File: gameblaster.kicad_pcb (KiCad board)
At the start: 2 copper layers, 136.7 x 109.8 mm, 74 parts, among them IC1 TEA2025, IC10 74LS125, IC12 74LS74, IC2 SAA1099, IC3 SAA1099, IC4 74LS245, IC5 74LS374, IC6 74LS138, IC7 74LS138, IC8 74LS32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

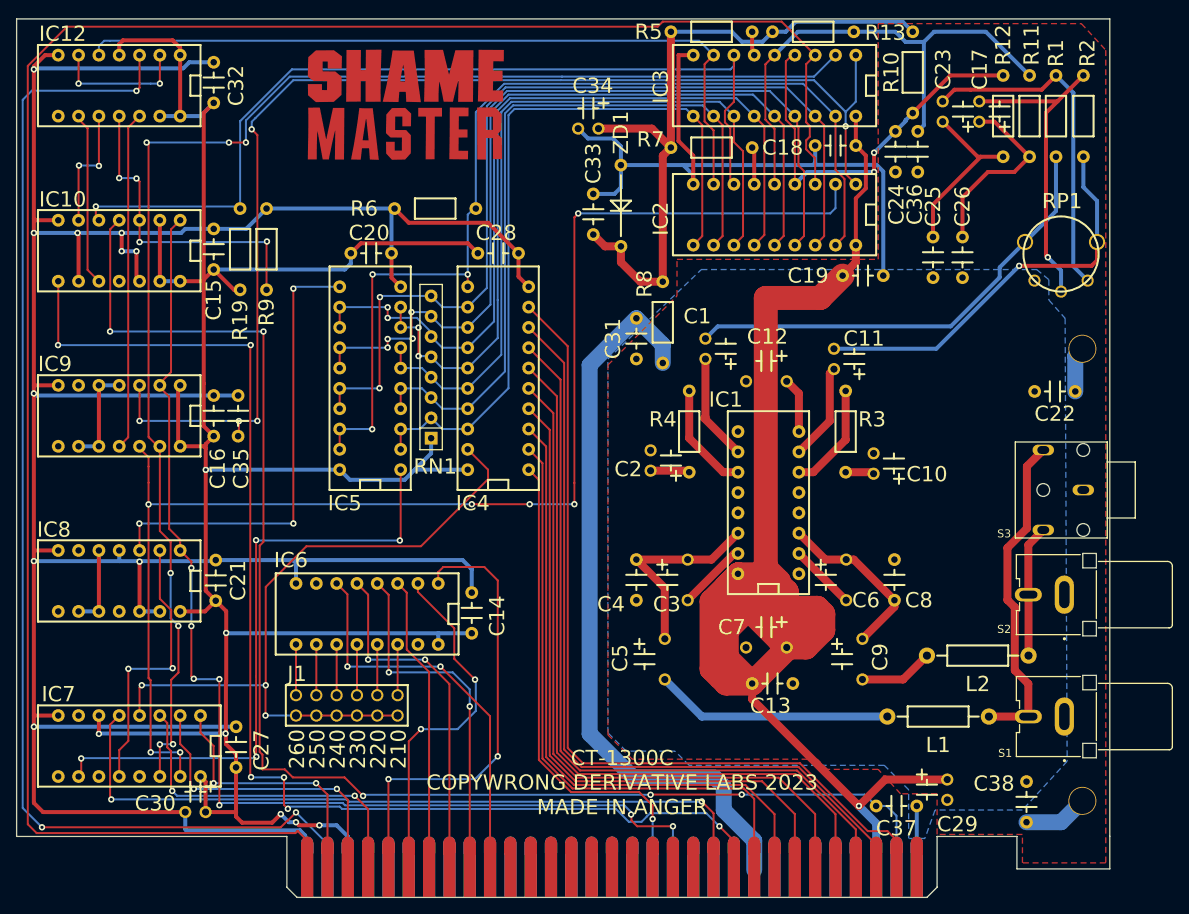
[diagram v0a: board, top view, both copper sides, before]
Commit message: fuck it let's add a big old digital ground plane
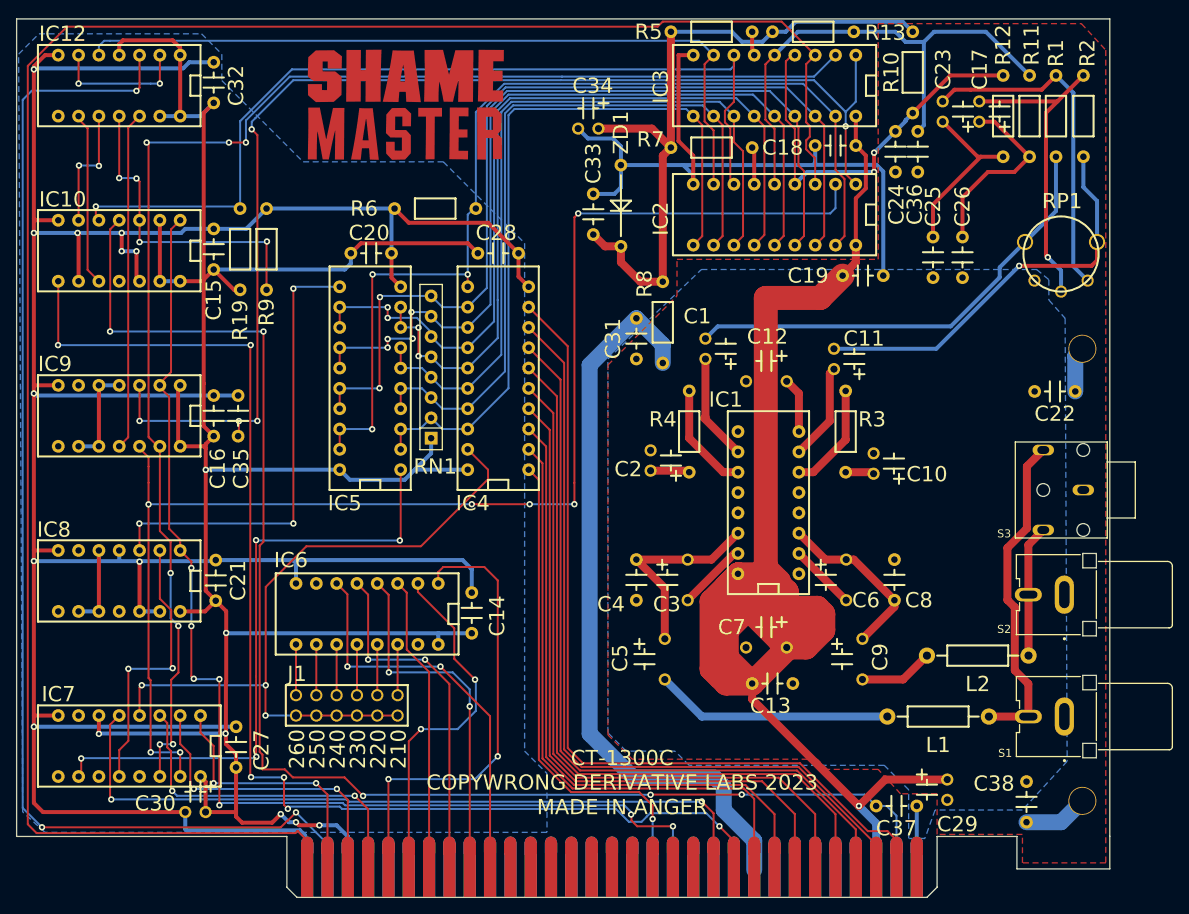
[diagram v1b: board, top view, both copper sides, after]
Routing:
- added copper zone on B.Cu, net GND
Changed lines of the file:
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@@
+    )
+  )
+  (zone (net 108) (net_name "GND") (layer "B.Cu") (hatch edge 0.508)
+    (connect_pads (clearance 0.508))
+    (min_thickness 0.254) (filled_areas_thickness no)
+    (fill yes (thermal_gap 0.508) (thermal_bridge_width 0.508))
+    (polygon
+      (pts
+        (xy 86.36 33.02)
+        (xy 86.36 36.322)
+        (xy 96.52 46.482)
+        (xy 114.046 46.482)
+        (xy 124.206 56.642)
+        (xy 124.206 120.142)
+        (xy 127 122.936)
+        (xy 127 130.302)
+        (xy 64.262 130.302)
+        (xy 61.468 127.762)
+        (xy 60.96 33.02)
+        (xy 63.5 30.48)
+        (xy 83.82 30.48)
+      )
     )
   )

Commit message: update gerbil
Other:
- board text added: "Special Thanks: TubeTime - reverse engineering of the original Game Blaster PCB; many circuits borrowed; footprint library. Tronix - original transceiver/register logic for card detection Wings - analog section consultation leaded solder - generally being a shithead and encouraging my terrible ideas"
- board text removed: "Special Thanks: TubeTime - reverse engineering of the big stupid DIP-40; DTACK circuit and TEA2025B section from the Snark Barker; copious footprints and silkscreen Tronix - original transceiver/register logic for card detection leadedsolder - generally being a shithead and encouraging my terrible ideas"
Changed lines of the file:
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@@
     (effects (font (size 1 1) (thickness 0.2)) (justify mirror))
   )
-  (gr_text "Special Thanks:\nTubeTime - reverse engineering of the\n  big stupid DIP-40; DTACK circuit and\n  TEA2025B section from the Snark Barker;\n  copious footprints and silkscreen\nTronix - original transceiver/register\n  logic for card detection\nleadedsolder - generally being a \n  shithead and encouraging my terrible\n  ideas" (at 128.27 38.1) (layer "B.SilkS")
+  (gr_text "Special Thanks:\nTubeTime - reverse engineering of the\n  original Game Blaster PCB; many circuits\n  borrowed; footprint library.\nTronix - original transceiver/register\n  logic for card detection\nWings - analog section consultation\nleaded solder - generally being a \n  shithead and encouraging my terrible\n  ideas" (at 128.27 38.1) (layer "B.SilkS")
     (effects (font (size 0.9525 0.9525) (thickness 0.127)) (justify left mirror))
   )

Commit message: Fix some shit
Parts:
- added R14: 1K, gameblaster:RESA400, F.Cu at (88.6, 52.3)
- C1, C11: value 0.22uF 16V -> 10uF 16V
- C10, C2: value 22uF 16V -> 10uF 16V
- C17, C23: value 1uF tant -> 10uF tant
- C24, C36: value 680pF -> 1000pF
- C25, C26: value 680pF -> 2200pF
- moved R19 39.8 mm to (128.3, 58.9)
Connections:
- C4 pad 2: Net-(C3-Pad1) -> Net-(C3-Pad2)
- C5 pad 1: Net-(C3-Pad1) -> Net-(C3-Pad2)
- C6 pad 2: Net-(C6-Pad2) -> Net-(C8-Pad1)
- C8 pad 1: Net-(C6-Pad1) -> Net-(C8-Pad1)
- C9 pad 1: Net-(C6-Pad1) -> Net-(C8-Pad1)
- IC1 pad 2: Net-(C6-Pad2) -> Net-(C8-Pad1)
- R19 pad 1: VCC -> VDDA
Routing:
- net /~{DTACK}: track 113.8 -> 138.7 mm, vias 1 -> 3
- net Net-(IC10-Pad6): track 15.6 -> 38.6 mm, vias 2 -> 3
- net Net-(C8-Pad1): track 0.00 -> 20.1 mm
- net Net-(C3-Pad1): track 25.4 -> 7.65 mm
- net Net-(C6-Pad1): track 21.9 -> 7.27 mm
- net Net-(C3-Pad2): track 8.71 -> 23.2 mm
- net Net-(C6-Pad2): track 8.33 -> 0.00 mm
- net VDDA: track 86.3 -> 94.0 mm
- net VCC: track 307.1 -> 302.7 mm

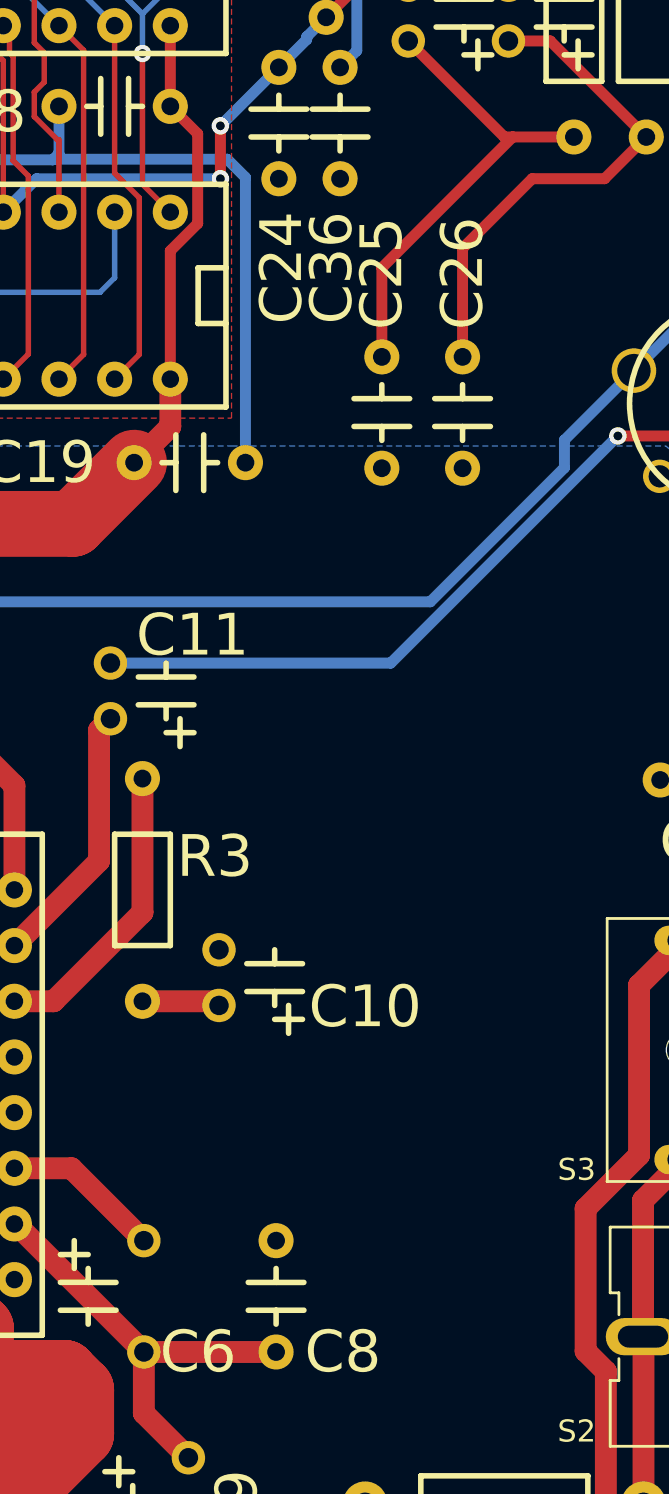
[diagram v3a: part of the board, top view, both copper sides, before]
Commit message: Add 3D models for Bracket and Volume pot/knob, update gerbers
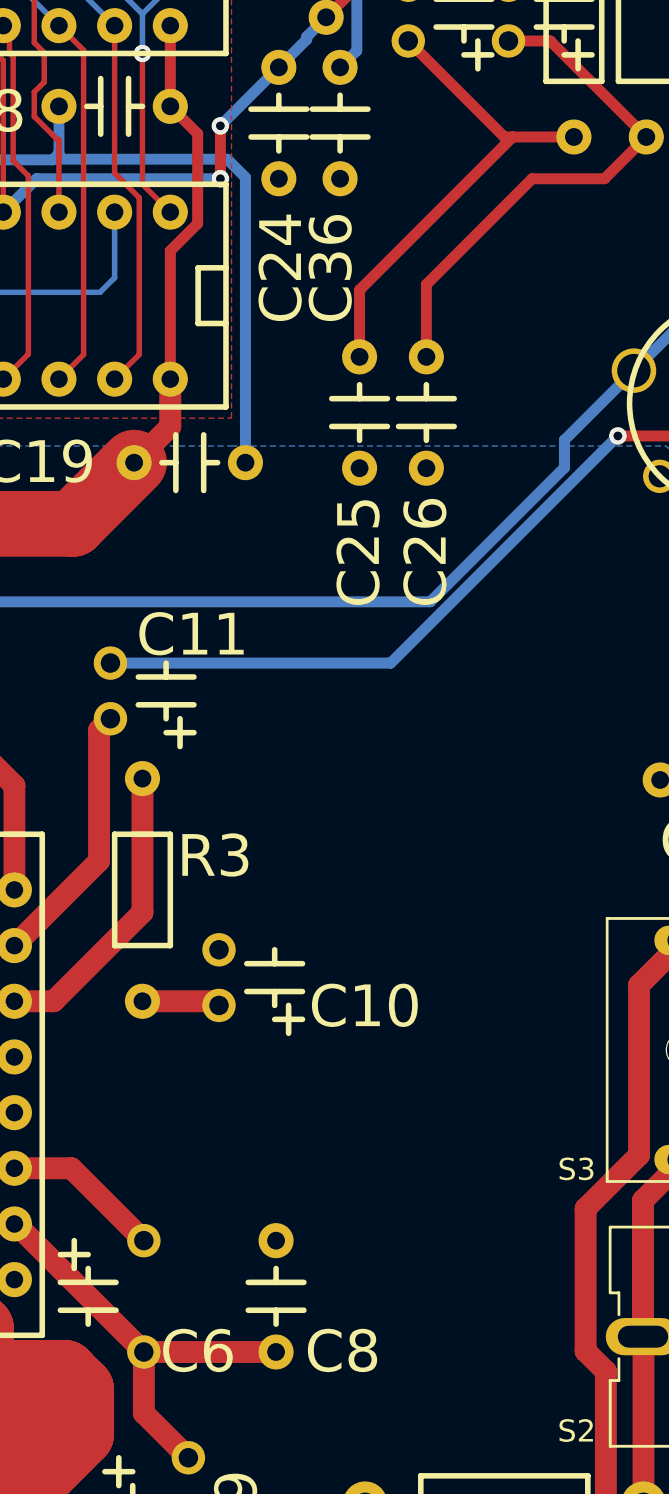
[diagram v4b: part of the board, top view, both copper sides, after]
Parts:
- C10, C2: value 10uF 16V -> 22uF 16V
- moved C26 1.65 mm to (177.3, 55.9)
- moved C25 1.02 mm to (174.2, 55.9)
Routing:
- net Net-(C17-Pad1): track 23.5 -> 24.2 mm
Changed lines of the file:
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@@
     (pad "1" thru_hole circle locked (at 0 56.515) (size 3.5 3.5) (drill 3.2766) (layers *.Cu *.Mask)
       (net 51 "/CHASSIS") (pinfunction "1") (pintype "input"))
-    (model "C:/Data/Projects/Adlib/mech/keystone 9202.wrl"
-      (offset (xyz 6.095999908 -88.26499867 6.476999903))
-      (scale (xyz 10 10 10))
-      (rotate (xyz 0 0 0))
+    (model "${KIPRJMOD}/packages3d/keystone-PN9202.STEP"
+      (offset (xyz 6.12 31.75 19.05))
+      (scale (xyz 1 1 1))
+      (rotate (xyz 0 180 90))
     )
   )
@@
     (pad "3B" thru_hole circle (at -3.323402 -3.323402 90) (size 1.524 1.524) (drill 1.016) (layers *.Cu *.Mask)
       (net 108 "Net-(C23-Pad2)") (pinfunction "3B") (pintype "passive"))
+    (model "${KIPRJMOD}/packages3d/RK08H12100F3.stp"
+      (offset (xyz 3.35 3.35 -0.125))
+      (scale (xyz 1 1 1))
+      (rotate (xyz 0 0 0))
+    )
+    (model "${KIPRJMOD}/packages3d/Volume-Knob-Recessed.step"
+      (offset (xyz 0 0 3.375))
+      (scale (xyz 1 1 1))
+      (rotate (xyz 0 0 0))
+    )
   )
   (footprint "gameblaster:RESA400" (layer "F.Cu")
@@
   )
   (footprint "gameblaster:CAPAC200" (layer "F.Cu")
-    (at 178.943 55.88 -90)
+    (at 177.292 55.88 -90)
     (property "Sheetfile" "gameblaster.kicad_sch")
     (property "Sheetname" "")
     (attr through_hole)
-    (fp_text reference "C26" (at -3.81 0 90) (layer "F.SilkS")
+    (fp_text reference "C26" (at 8.89 0 90) (layer "F.SilkS")
       (effects (font (size 1.905 1.905) (thickness 0.254)))
     )
@@
   )
   (footprint "gameblaster:CAPAC200" (layer "F.Cu")
-    (at 175.26 55.88 -90)
+    (at 174.244 55.88 -90)
     (property "Sheetfile" "gameblaster.kicad_sch")
     (property "Sheetname" "")
     (attr through_hole)
-    (fp_text reference "C25" (at -3.81 0 90) (layer "F.SilkS")
+    (fp_text reference "C25" (at 8.89 0 90) (layer "F.SilkS")
       (effects (font (size 1.905 1.905) (thickness 0.254)))
     )
@@
       (effects (font (size 1.905 1.905) (thickness 0.254)))
     )
-    (fp_text value "10uF 16V" (at 1.397 1.5875 90) (layer "F.Fab")
+    (fp_text value "22uF 16V" (at 1.397 1.5875 90) (layer "F.Fab")
       (effects (font (size 1 1) (thickness 0.15)))
     )
@@
       (effects (font (size 1.905 1.905) (thickness 0.254)))
     )
-    (fp_text value "10uF 16V" (at 1.27 -4.699 90) (layer "F.Fab")
+    (fp_text value "22uF 16V" (at 1.27 -4.699 90) (layer "F.Fab")
       (effects (font (size 1 1) (thickness 0.15)))
     )
@@
       (xy 113.880473 39.712815)
     ) (layer "F.Mask") (width 0) (fill solid))
-  (gr_circle (center 191.262 58.006) (end 201.512 58.006) (layer "Dwgs.User") (width 0.2) (fill none))
+  (gr_circle (center 191.262 58.006) (end 203.262 58.006) (layer "Dwgs.User") (width 0.2) (fill none))
   (gr_line (start 197.358 28.618) (end 60.706 28.618) (layer "Edge.Cuts") (width 0.15))
   (gr_line (start 175.768 137.16) (end 175.768 130.81) (layer "Edge.Cuts") (width 0.15))
@@
   (segment (start 158.496 80.2005) (end 158.496 75.438) (width 1) (layer "F.Cu") (net 49))
   (segment (start 158.496 75.438) (end 156.972 73.914) (width 1) (layer "F.Cu") (net 49))
-  (segment (start 182.118 47.752) (end 178.943 50.927) (width 0.5) (layer "F.Cu") (net 50))
-  (segment (start 178.943 50.927) (end 178.943 55.88) (width 0.5) (layer "F.Cu") (net 50))
-  (segment (start 181.0385 41.4655) (end 182.9435 41.4655) (width 0.5) (layer "F.Cu") (net 50))
-  (segment (start 182.9435 41.4655) (end 187.325 45.847) (width 0.5) (layer "F.Cu") (net 50))
   (segment (start 187.325 45.847) (end 185.42 47.752) (width 0.5) (layer "F.Cu") (net 50))
+  (segment (start 181.0385 41.4655) (end 182.9435 41.4655) (width 0.5) (layer "F.Cu") (net 50))
   (segment (start 185.42 47.752) (end 182.118 47.752) (width 0.5) (layer "F.Cu") (net 50))
+  (segment (start 182.9435 41.4655) (end 187.325 45.847) (width 0.5) (layer "F.Cu") (net 50))
+  (segment (start 177.292 52.578) (end 177.292 55.88) (width 0.5) (layer "F.Cu") (net 50))
+  (segment (start 182.118 47.752) (end 177.292 52.578) (width 0.5) (layer "F.Cu") (net 50))
   (segment (start 186.944 129.032) (end 191.262 129.032) (width 2) (layer "B.Cu") (net 51))
   (segment (start 193.04 70.739) (end 193.929 69.85) (width 2) (layer "B.Cu") (net 51))
@@
   (segment (start 181.229 45.847) (end 184.023 45.847) (width 0.5) (layer "F.Cu") (net 70))
   (segment (start 176.4665 41.4655) (end 180.848 45.847) (width 0.5) (layer "F.Cu") (net 70))
+  (segment (start 174.244 52.832) (end 174.244 55.88) (width 0.5) (layer "F.Cu") (net 70))
+  (segment (start 181.229 45.847) (end 174.244 52.832) (width 0.5) (layer "F.Cu") (net 70))
   (segment (start 180.848 45.847) (end 181.229 45.847) (width 0.5) (layer "F.Cu") (net 70))
-  (segment (start 175.26 55.88) (end 175.26 51.816) (width 0.5) (layer "F.Cu") (net 70))
-  (segment (start 175.26 51.816) (end 181.229 45.847) (width 0.5) (layer "F.Cu") (net 70))
   (segment (start 76.073 37.2364) (end 75.692 37.6174) (width 0.25) (layer "F.Cu") (net 71))
   (segment (start 76.073 33.147) (end 76.073 37.2364) (width 0.25) (layer "F.Cu") (net 71))
@@
   (segment (start 158.496 95.4405) (end 158.5595 95.4405) (width 1) (layer "F.Cu") (net 131))
   (segment (start 164.4015 101.2825) (end 170.434 101.2825) (width 1) (layer "F.Cu") (net 131))
-  (segment (start 164.4015 101.2825) (end 164.338 101.2825) (width 1) (layer "F.Cu") (net 131))
   (segment (start 164.4015 101.2825) (end 164.4015 104.0765) (width 1) (layer "F.Cu") (net 131))
   (segment (start 164.4015 104.0765) (end 166.4335 106.1085) (width 1) (layer "F.Cu") (net 131))
